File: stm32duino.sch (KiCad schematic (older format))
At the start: 19 parts, among them P1 RF7021SE, P2 DISP_I2C, P3 DISP_SER, P4 HOST_SER, U1 stm32f103c8t6-module-china

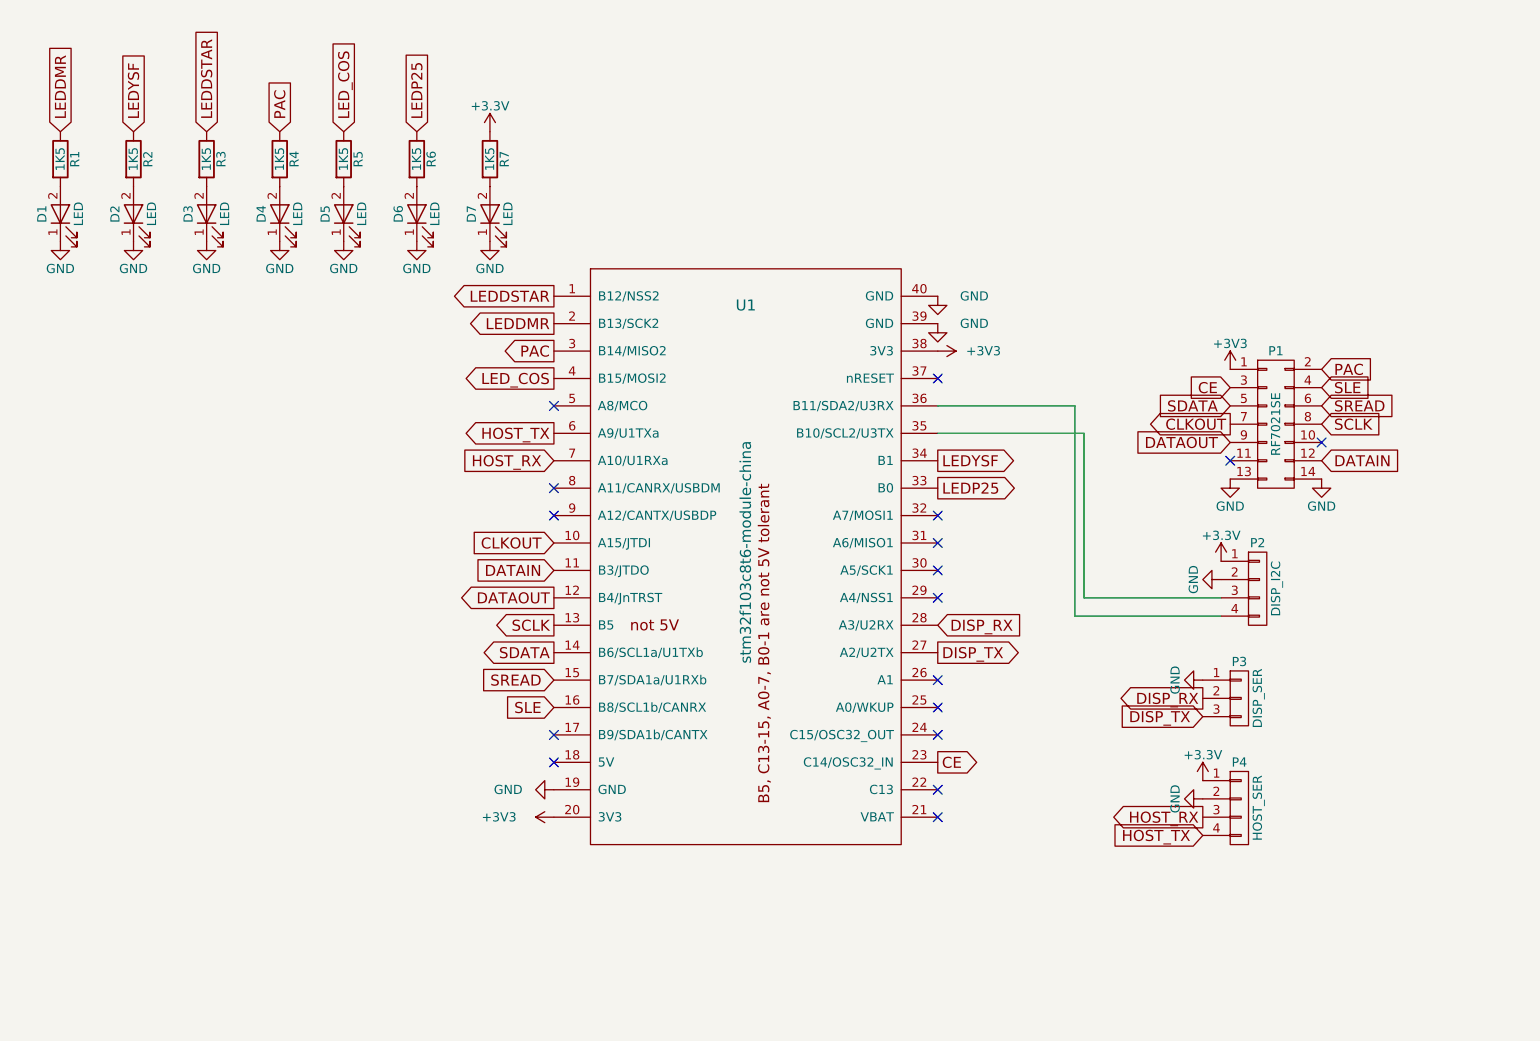
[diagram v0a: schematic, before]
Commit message: modified for Trhuhole components, added NXD LED.
Modifications from original Project:
-Changed LEDs and resistors from SMD to TrhuHole, and facing to the front of the board.
-Added LED for NXD operation.
-Increased track width for RF7021SE +3.3 VDC.
-Modified header connectors orientation for 3D view.
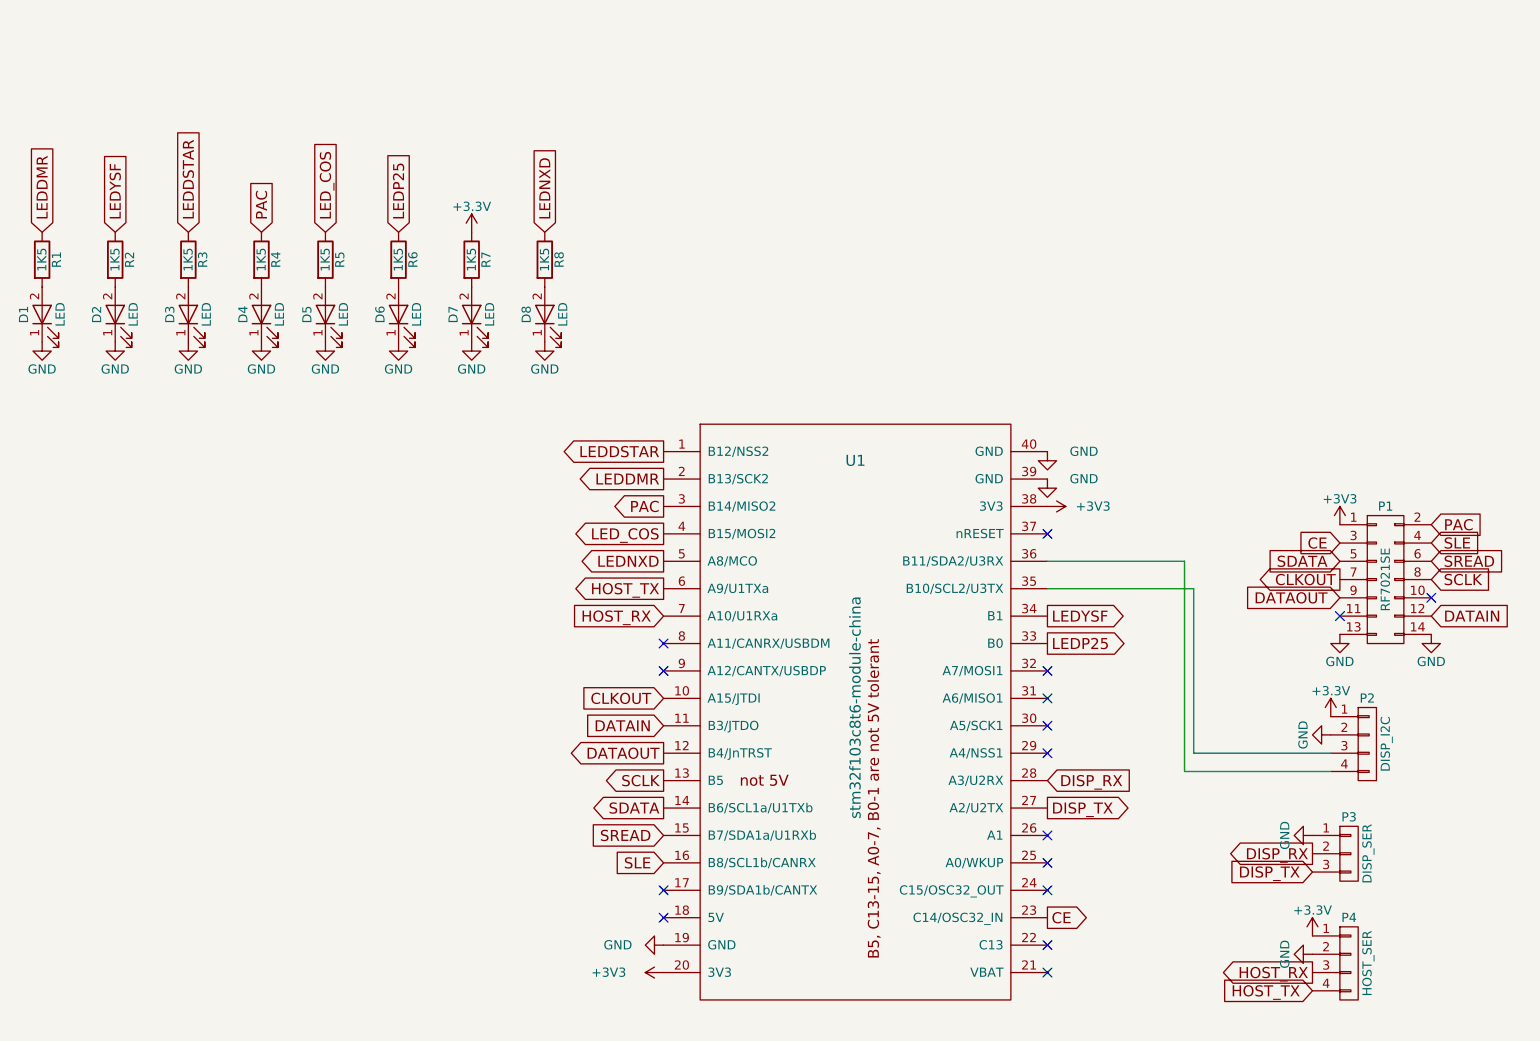
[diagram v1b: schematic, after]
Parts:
- added D8: LED, LEDs:LED-3MM, symbol LED
- added R8: 1K5, Resistors_THT:R_Axial_DIN0204_L3.6mm_D1.6mm_P5.08mm_Horizontal, symbol R
- D1, D2, D3, D4, D5, D6, D7: footprint LEDs:LED_0805 -> LEDs:LED-3MM
- R1, R2, R3, R4, R5, R6, R7: footprint Resistors_SMD:R_0805 -> Resistors_THT:R_Axial_DIN0204_L3.6mm_D1.6mm_P5.08mm_Horizontal
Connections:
- net GND: now also D8.1 (K)
- net LEDNXD: now reaches U1.5 (A8/MCO)
- net LEDNXD: now also R8.1
- new net: D8.2 (A), R8.2
- no-connect marks 17 -> 16
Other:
- moved on the sheet: D1, D2, D3, D4, D5, D6, D7, P1, P2, P3, P4, R1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

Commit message: Added Mounting holes and RF7021 breakout board footprint
Additions: 3.5mm mounting holes on corners., footprint for RF7021 breakout board, Text labels for CC licensing, model, usage and credits, text labels for LED indicator signals.
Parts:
- P1: footprint Pin_Headers:Pin_Header_Straight_2x07_Pitch2.54mm -> RF_Modules:RF7021SE_Breakout
- P2, P4: footprint Pin_Headers:Pin_Header_Angled_1x04_Pitch2.54mm -> Pin_Headers:Pin_Header_Straight_1x04_Pitch2.54mm
- P3: footprint Pin_Headers:Pin_Header_Angled_1x03_Pitch2.54mm -> Pin_Headers:Pin_Header_Straight_1x03_Pitch2.54mm
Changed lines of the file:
@@
 F 0 "P1" H 8650 3850 50  0000 C CNN
 F 1 "RF7021SE" V 8650 3450 50  0000 C CNN
-F 2 "Pin_Headers:Pin_Header_Straight_2x07_Pitch2.54mm" H 8650 2250 50  0001 C CNN
+F 2 "RF_Modules:RF7021SE_Breakout" H 8650 2250 50  0001 C CNN
 F 3 "" H 8650 2250 50  0000 C CNN
 	1    8650 3450
@@
 F 0 "P2" H 8550 4600 50  0000 C CNN
 F 1 "DISP_I2C" V 8650 4350 50  0000 C CNN
-F 2 "Pin_Headers:Pin_Header_Angled_1x04_Pitch2.54mm" H 8550 4350 50  0001 C CNN
+F 2 "Pin_Headers:Pin_Header_Straight_1x04_Pitch2.54mm" H 8550 4350 50  0001 C CNN
 F 3 "" H 8550 4350 50  0000 C CNN
 	1    8550 4350
@@
 F 0 "P3" H 8450 5150 50  0000 C CNN
 F 1 "DISP_SER" V 8550 4950 50  0000 C CNN
-F 2 "Pin_Headers:Pin_Header_Angled_1x03_Pitch2.54mm" H 8450 4950 50  0001 C CNN
+F 2 "Pin_Headers:Pin_Header_Straight_1x03_Pitch2.54mm" H 8450 4950 50  0001 C CNN
 F 3 "" H 8450 4950 50  0000 C CNN
 	1    8450 4950
@@
 F 0 "P4" H 8450 5800 50  0000 C CNN
 F 1 "HOST_SER" V 8550 5550 50  0000 C CNN
-F 2 "Pin_Headers:Pin_Header_Angled_1x04_Pitch2.54mm" H 8450 5550 50  0001 C CNN
+F 2 "Pin_Headers:Pin_Header_Straight_1x04_Pitch2.54mm" H 8450 5550 50  0001 C CNN
 F 3 "" H 8450 5550 50  0000 C CNN
 	1    8450 5550
